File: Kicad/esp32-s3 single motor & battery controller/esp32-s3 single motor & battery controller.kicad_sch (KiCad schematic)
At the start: 58 parts, among them J1 JST SH SM04B, J2 7 pin FPC 0.3mm, SW1 SW_Push, SW2 SW_Push, U5 ESP32-S3, U6 74HC595, Y1 40mhz, 10ppm

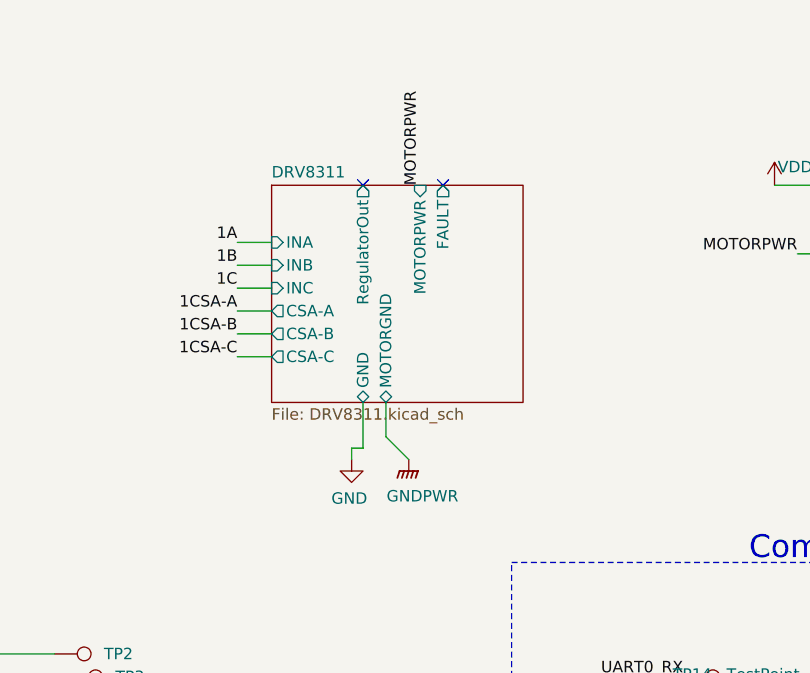
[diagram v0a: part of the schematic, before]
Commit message: Started migrating driver to the back of the motor
If successful, this will save a ton of space. This will be a mess for awhile.
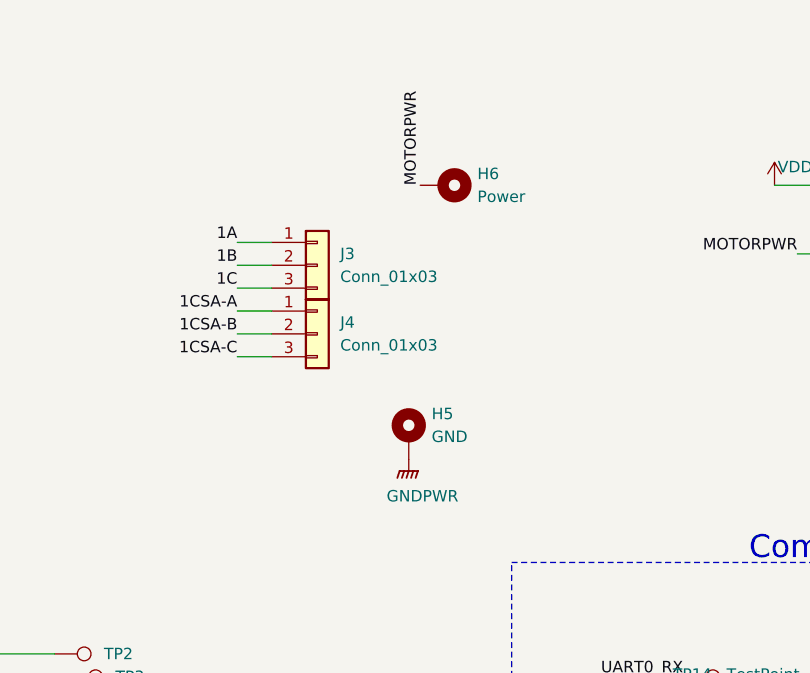
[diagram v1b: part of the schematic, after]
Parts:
- added H5: GND, symbol Mechanical:MountingHole_Pad
- added H6: Power, symbol Mechanical:MountingHole_Pad
- added J3, J4: Conn_01x03, symbol Connector_Generic:Conn_01x03
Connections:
- net 1A: now also J3.1 (Pin_1)
- net 1B: now also J3.2 (Pin_2)
- net 1C: now also J3.3 (Pin_3)
- net 1CSA-A: now also J4.1 (Pin_1)
- net 1CSA-B: now also J4.2 (Pin_2)
- net 1CSA-C: now also J4.3 (Pin_3)
- net GNDPWR: now also H5.1
- net MOTORPWR: now also H6.1
- no-connect marks 20 -> 18
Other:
- removed sheet DRV8311

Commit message: Mostly finished Mainboard, adding silkscreen to magnetic encoder
I added pin headers to support my external driver board, and shrunk the whole design
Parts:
- H5, H6: footprint (none) -> TestPoint:TestPoint_Pad_D2.0mm
- J3, J4: footprint (none) -> Connector_PinHeader_1.27mm:PinHeader_1x03_P1.27mm_Vertical
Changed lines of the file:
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@@
 			)
 		)
-		(property "Footprint" ""
+		(property "Footprint" "TestPoint:TestPoint_Pad_D2.0mm"
 			(at 165.1 59.69 0)
 			(effects
@@
 			)
 		)
-		(property "Footprint" ""
+		(property "Footprint" "Connector_PinHeader_1.27mm:PinHeader_1x03_P1.27mm_Vertical"
 			(at 154.94 48.26 0)
 			(effects
@@
 			)
 		)
-		(property "Footprint" ""
+		(property "Footprint" "Connector_PinHeader_1.27mm:PinHeader_1x03_P1.27mm_Vertical"
 			(at 154.94 40.64 0)
 			(effects
@@
 			)
 		)
-		(property "Footprint" ""
+		(property "Footprint" "TestPoint:TestPoint_Pad_D2.0mm"
 			(at 168.91 31.75 0)
 			(effects
@@
 		)
 		(instances
-			(project "esp32-s3 and DRV8311 single motor board"
+			(project "esp32-s3 single motor & battery controller"
 				(path "/eb3f183d-8bb1-43a5-a363-092ed67891e3"
 					(page "3")

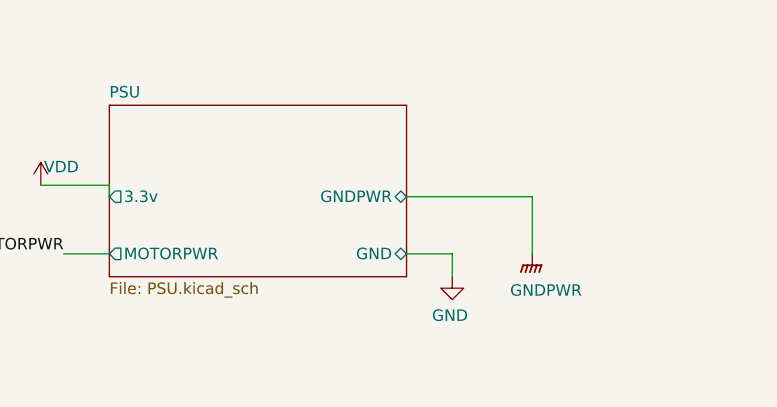
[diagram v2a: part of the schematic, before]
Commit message: Finished charger, added balancer circuitry
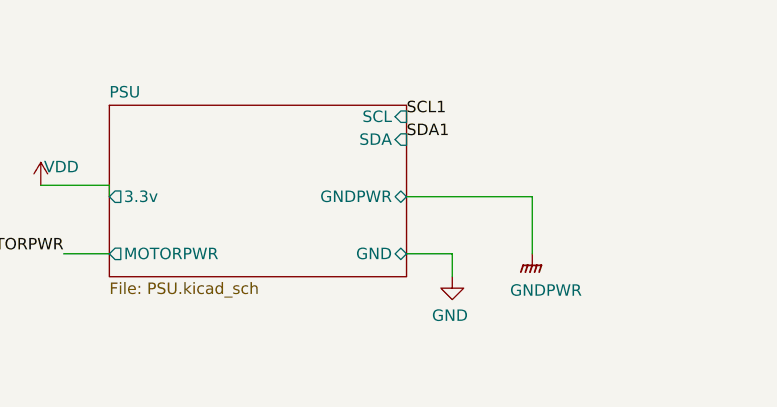
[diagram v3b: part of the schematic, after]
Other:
- sheet PSU ports: added SCL, SDA; removed none
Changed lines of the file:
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@@
 		)
 	)
+	(label "SCL1"
+		(at 246.38 24.13 0)
+		(fields_autoplaced yes)
+		(effects
+			(font
+				(size 1.27 1.27)
+			)
+			(justify left bottom)
+		)
+	)
 	(label "1CSA-A"
 		(at 161.29 118.11 180)
@@
 		)
 	)
+	(label "SDA1"
+		(at 246.38 26.67 0)
+		(fields_autoplaced yes)
+		(effects
+			(font
+				(size 1.27 1.27)
+			)
+			(justify left bottom)
+		)
+	)
 	(label "MOTORPWR"
 		(at 71.12 166.37 180)
@@
 			)
 		)
+		(pin "SCL" input
+			(at 246.38 24.13 0)
+			(effects
+				(font
+					(size 1.27 1.27)
+				)
+				(justify right)
+			)
+		)
+		(pin "SDA" input
+			(at 246.38 26.67 0)
+			(effects
+				(font
+					(size 1.27 1.27)
+				)
+				(justify right)
+			)
+		)

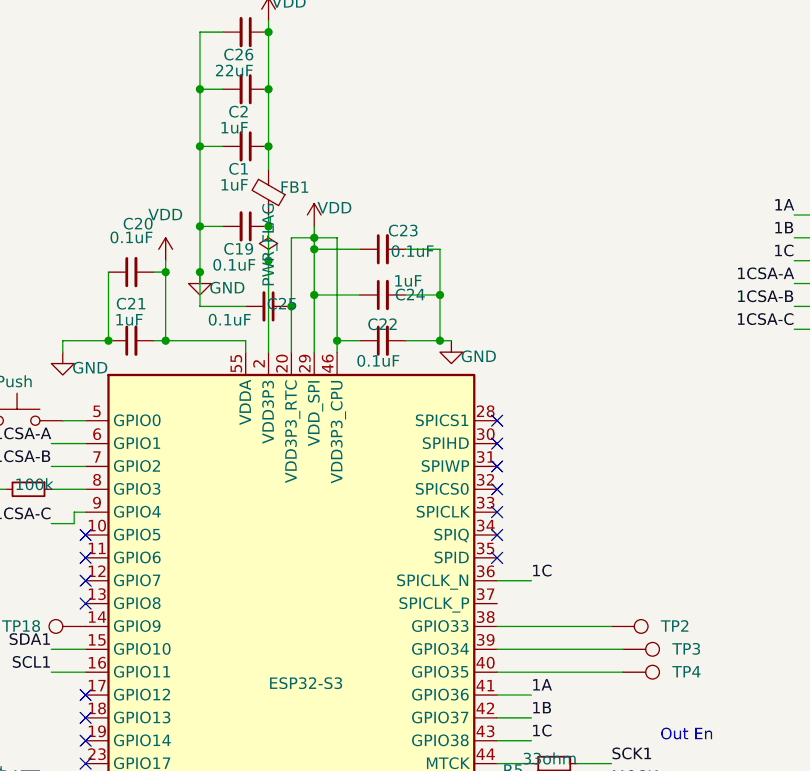
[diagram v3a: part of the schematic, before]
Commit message: Finished PSU schematic, Fixed ERC errors
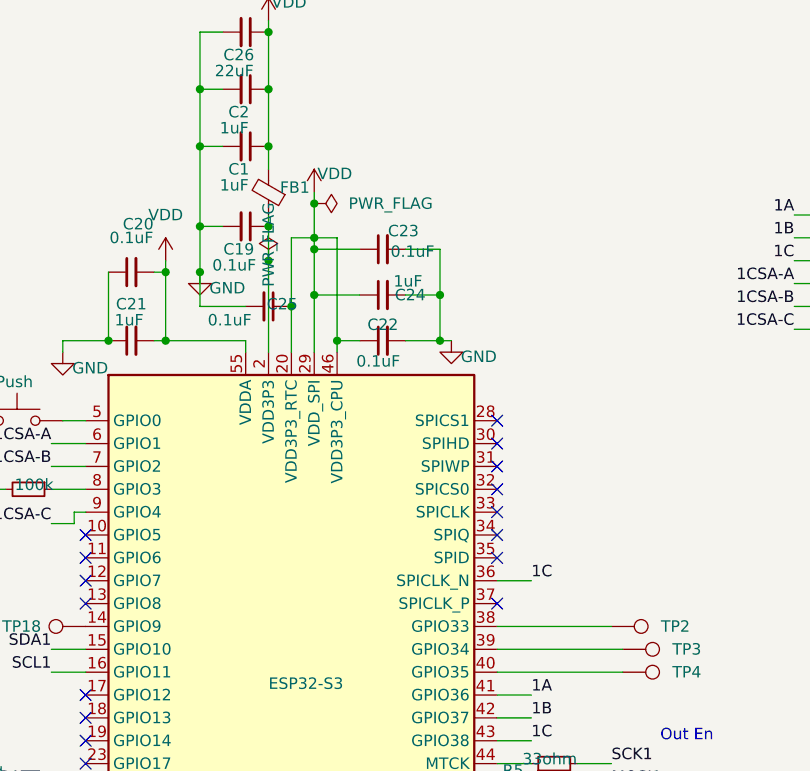
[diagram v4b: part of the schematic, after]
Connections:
- net GND: no longer U6.17 (Pad)
- no-connect marks 18 -> 19
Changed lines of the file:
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@@
 	)
 	(junction
+		(at 92.71 36.83)
+		(diameter 0)
+		(color 0 0 0 0)
+	)
+	(junction
 		(at 53.34 123.19)
 		(diameter 0)
@@
 	)
 	(no_connect
+		(at 113.03 81.28)
+	)
+	(no_connect
 		(at 67.31 73.66)
 	)
@@
 	(wire
 		(pts
-			(xy 92.71 39.37) (xy 92.71 40.64)
+			(xy 92.71 35.56) (xy 92.71 36.83)
 		)
 		(stroke
@@
 	(wire
 		(pts
+			(xy 92.71 36.83) (xy 92.71 40.64)
+		)
+		(stroke
+			(width 0)
+			(type default)
+		)
+	)
+	(wire
+		(pts
 			(xy 40.64 107.95) (xy 43.18 107.95)
 		)
@@
 	(symbol
 		(lib_id "power:VDD")
-		(at 92.71 39.37 0)
+		(at 92.71 35.56 0)
 		(unit 1)
 		(exclude_from_sim no)
@@
 		(dnp no)
 		(property "Reference" "#PWR04"
-			(at 92.71 43.18 0)
+			(at 92.71 39.37 0)
 			(effects
 				(font
@@
 		)
 		(property "Value" "VDD"
-			(at 94.996 37.338 0)
+			(at 94.996 33.528 0)
 			(effects
 				(font
@@
 		)
 		(property "Footprint" ""
-			(at 92.71 39.37 0)
+			(at 92.71 35.56 0)
 			(effects
 				(font
@@
 		)
 		(property "Datasheet" ""
-			(at 92.71 39.37 0)
+			(at 92.71 35.56 0)
 			(effects
 				(font
@@
 		)
 		(property "Description" "Power symbol creates a global label with name \"VDD\""
-			(at 92.71 39.37 0)
+			(at 92.71 35.56 0)
 			(effects
 				(font
@@
 	)
 	(symbol
+		(lib_id "power:PWR_FLAG")
+		(at 92.71 36.83 270)
+		(unit 1)
+		(exclude_from_sim no)
+		(in_bom yes)
+		(on_board yes)
+		(dnp no)
+		(fields_autoplaced yes)
+		(property "Reference" "#FLG03"
+			(at 94.615 36.83 0)
+			(effects
+				(font
+					(size 1.27 1.27)
+				)
+				(hide yes)
+			)
+		)
+		(property "Value" "PWR_FLAG"
+			(at 96.52 36.8299 90)
+			(effects
+				(font
+					(size 1.27 1.27)
+				)
+				(justify left)
+			)
+		)
+		(property "Footprint" ""
+			(at 92.71 36.83 0)
+			(effects
+				(font
+					(size 1.27 1.27)
+				)
+				(hide yes)
+			)
+		)
+		(property "Datasheet" "~"
+			(at 92.71 36.83 0)
+			(effects
+				(font
+					(size 1.27 1.27)
+				)
+				(hide yes)
+			)
+		)
+		(property "Description" "Special symbol for telling ERC where power comes from"
+			(at 92.71 36.83 0)
+			(effects
+				(font
+					(size 1.27 1.27)
+				)
+				(hide yes)
+			)
+		)
+		(pin "1"
+		)
+		(instances
+			(project "esp32-s3 single motor & battery controller"
+				(path "/eb3f183d-8bb1-43a5-a363-092ed67891e3"
+					(reference "#FLG03")
+					(unit 1)
+				)
+			)
+		)
+	)
+	(symbol
 		(lib_id "power:GND")
 		(at 49.53 68.58 0)
@@
 		(pin "10"
 		)
-		(pin "17"
-		)
 		(instances

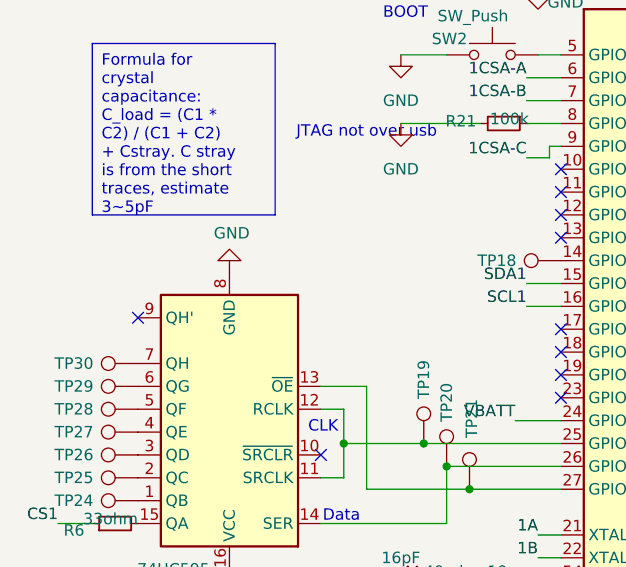
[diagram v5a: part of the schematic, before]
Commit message: Running DRC and fixing footprints
I had to fix the footprints of the driver chip and the shift register, because there were some undefined pads and the vias were too small.
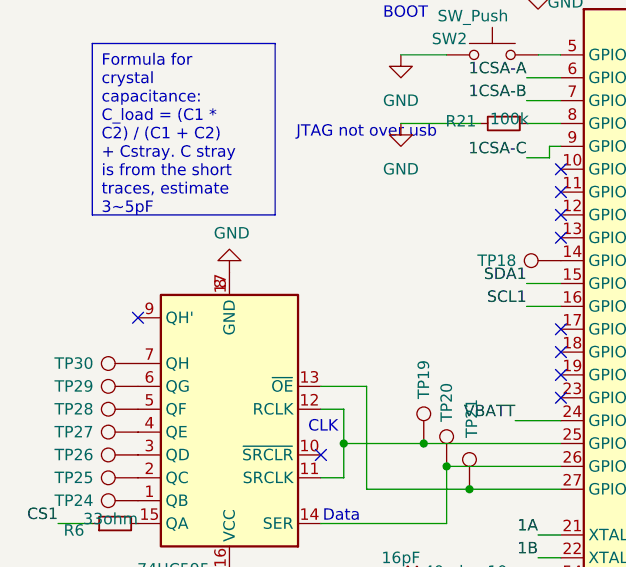
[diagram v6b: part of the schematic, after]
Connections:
- net GND: now also U6.17 (GND)
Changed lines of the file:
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@@
 		(pin "10"
+		)
+		(pin "17"
 		)
 		(instances

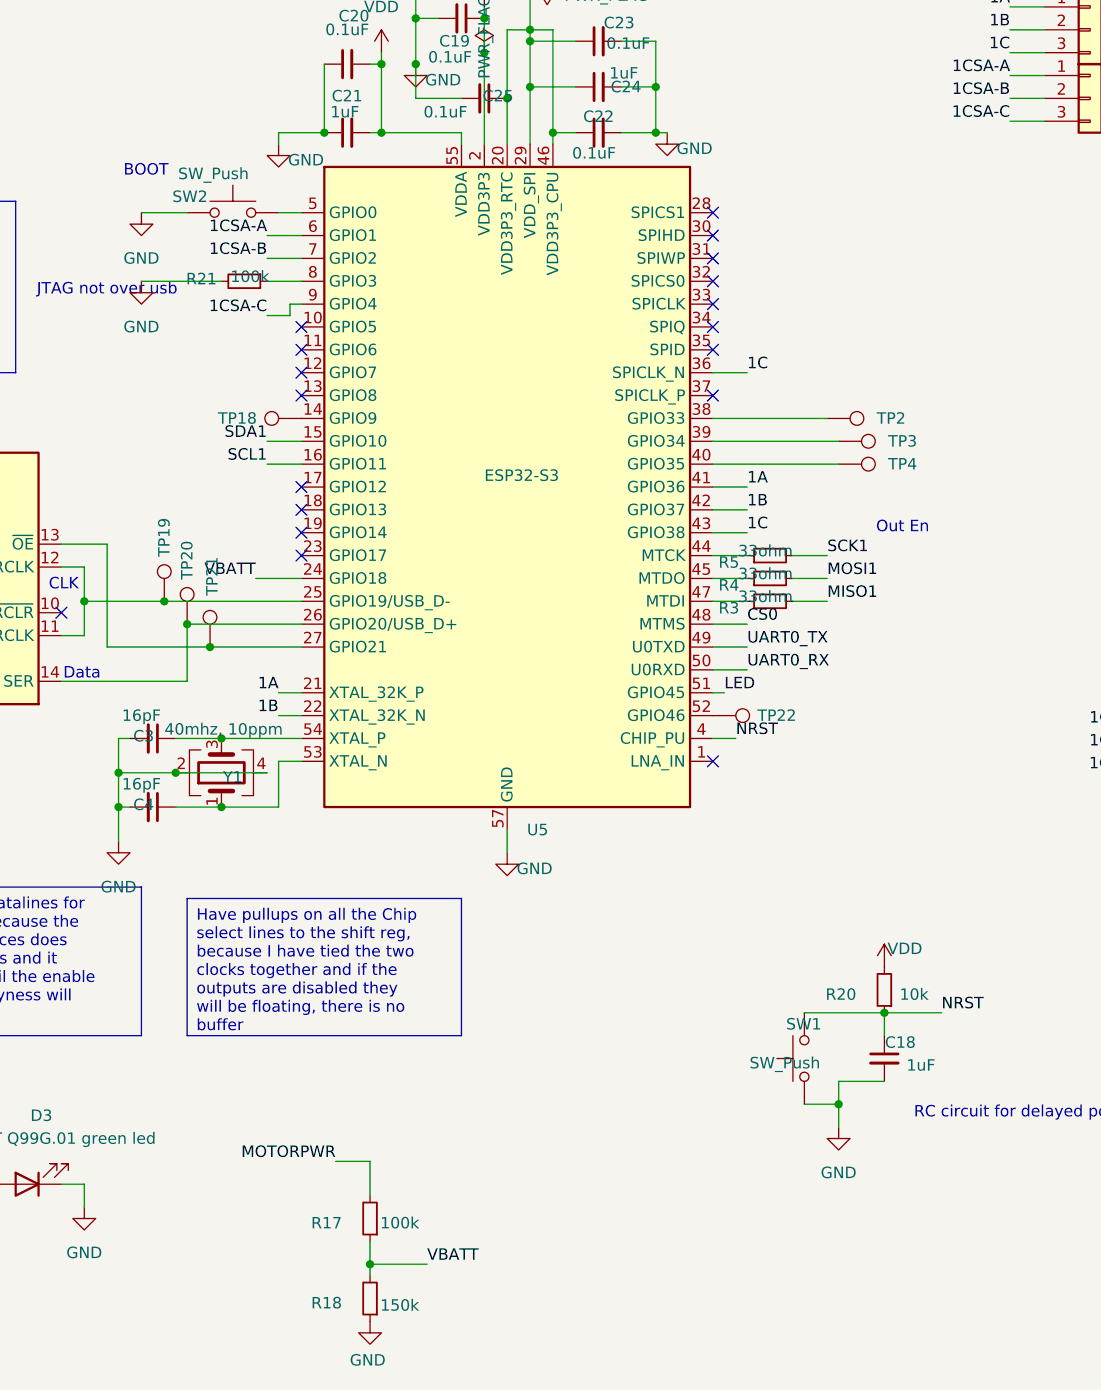
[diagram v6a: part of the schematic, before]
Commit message: Removed battery voltage divider, fixed BATTPres indicator
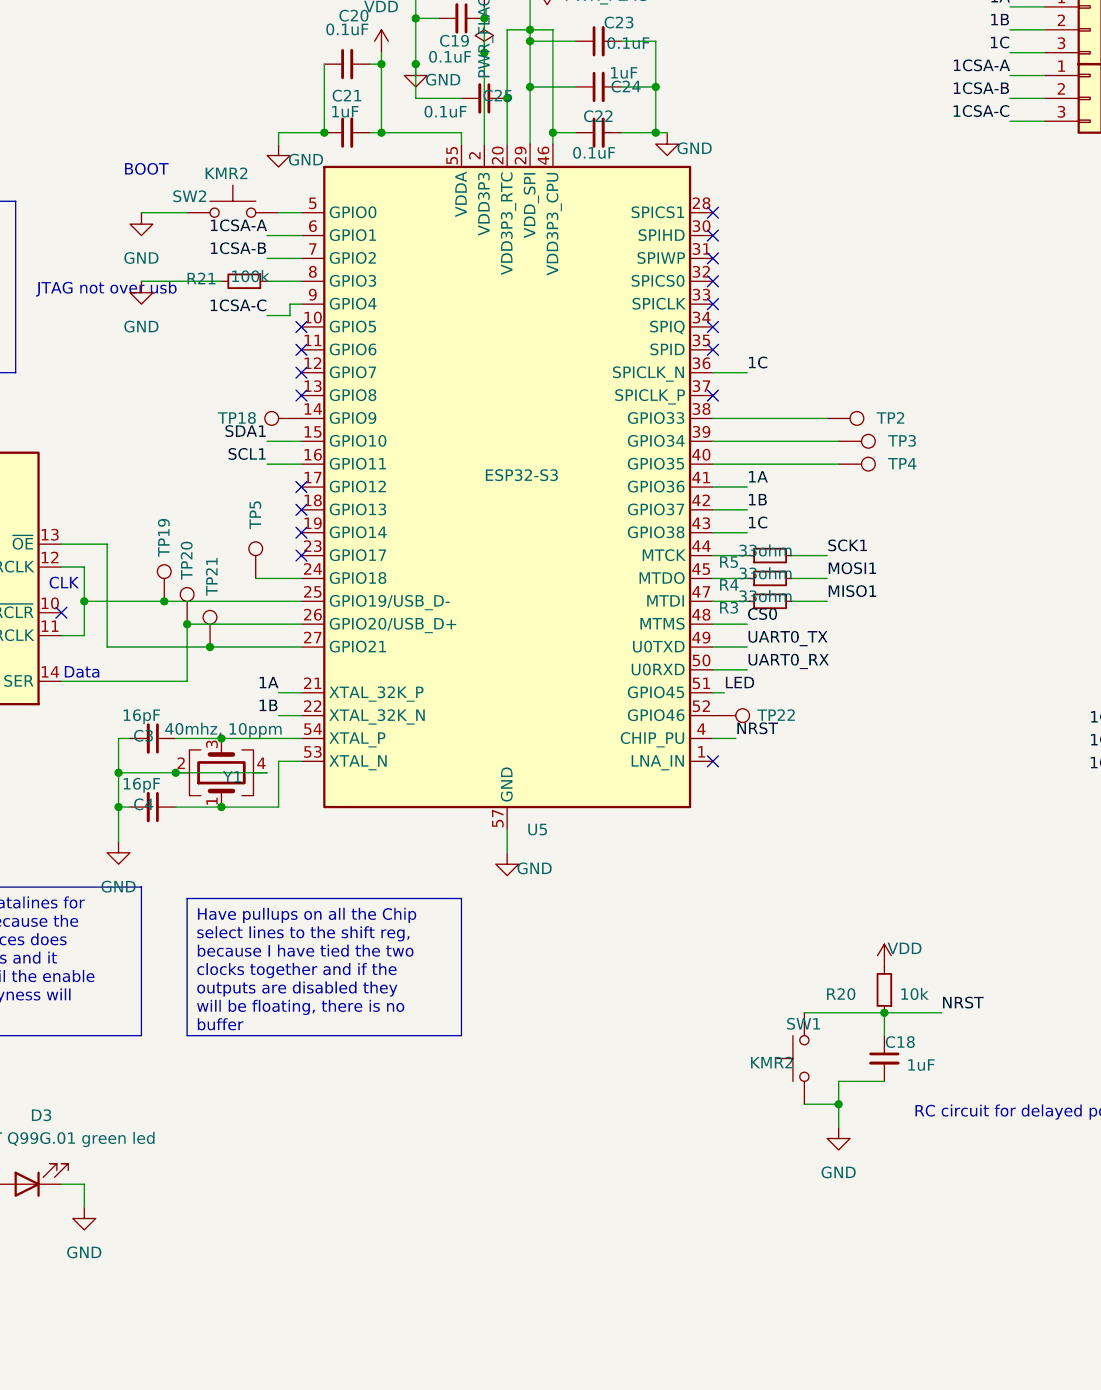
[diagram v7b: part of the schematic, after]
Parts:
- removed R17: 100k, Resistor_SMD:R_0603_1608Metric, symbol Device:R_Small
- removed R18: 150k, Resistor_SMD:R_0603_1608Metric, symbol Device:R_Small
- added TP5: ~, TestPoint:TestPoint_Pad_D1.0mm, symbol Connector:TestPoint
- SW1, SW2: value SW_Push -> KMR2
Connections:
- net VBATT: no longer names the net of U5.24 (GPIO18)
- net VBATT: now also TP5.1
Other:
- note removed: "Out En"

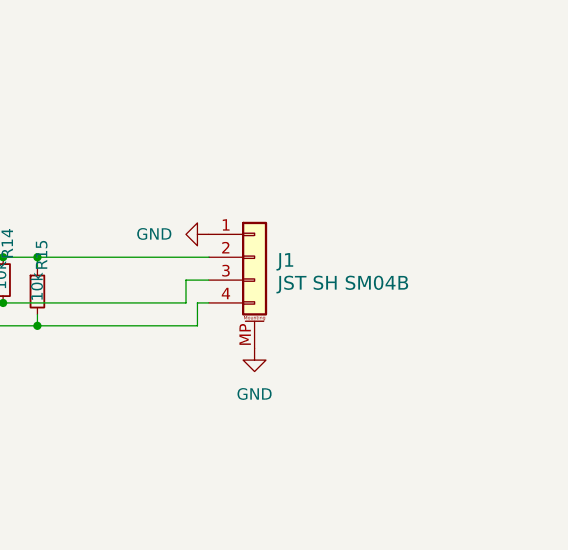
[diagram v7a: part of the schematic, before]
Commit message: Finished design
I speced out the proper diodes, routed the wires away from the inductor, added more ground vias, and did some general cleanup.
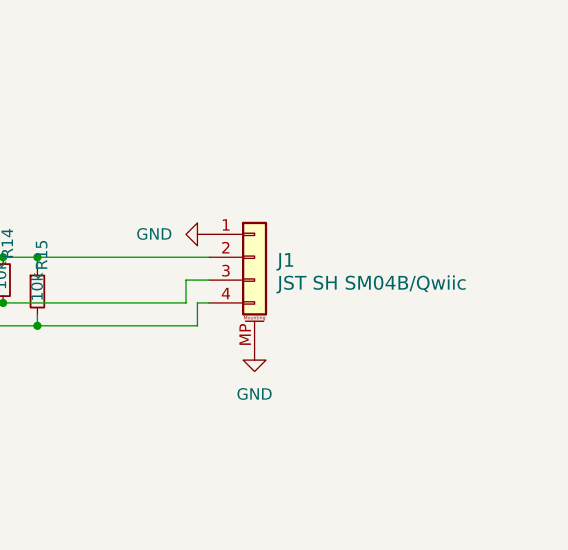
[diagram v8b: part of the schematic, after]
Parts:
- J1: value JST SH SM04B -> JST SH SM04B/Qwiic
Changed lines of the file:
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@@
 			)
 		)
-		(property "Value" "JST SH SM04B"
+		(property "Value" "JST SH SM04B/Qwiic"
 			(at 255.27 150.2155 0)
 			(effects
